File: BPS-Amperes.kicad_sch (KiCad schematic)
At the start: 35 parts, among them J1 Conn_02x10_Odd_Even, J2 ShuntConn, J3 PassthroughConn, J4 TestConn, J5 Conn_01x02, U1 INA186A3IDDFT, U2 OPA2196, U4 REF1930AIDDCT

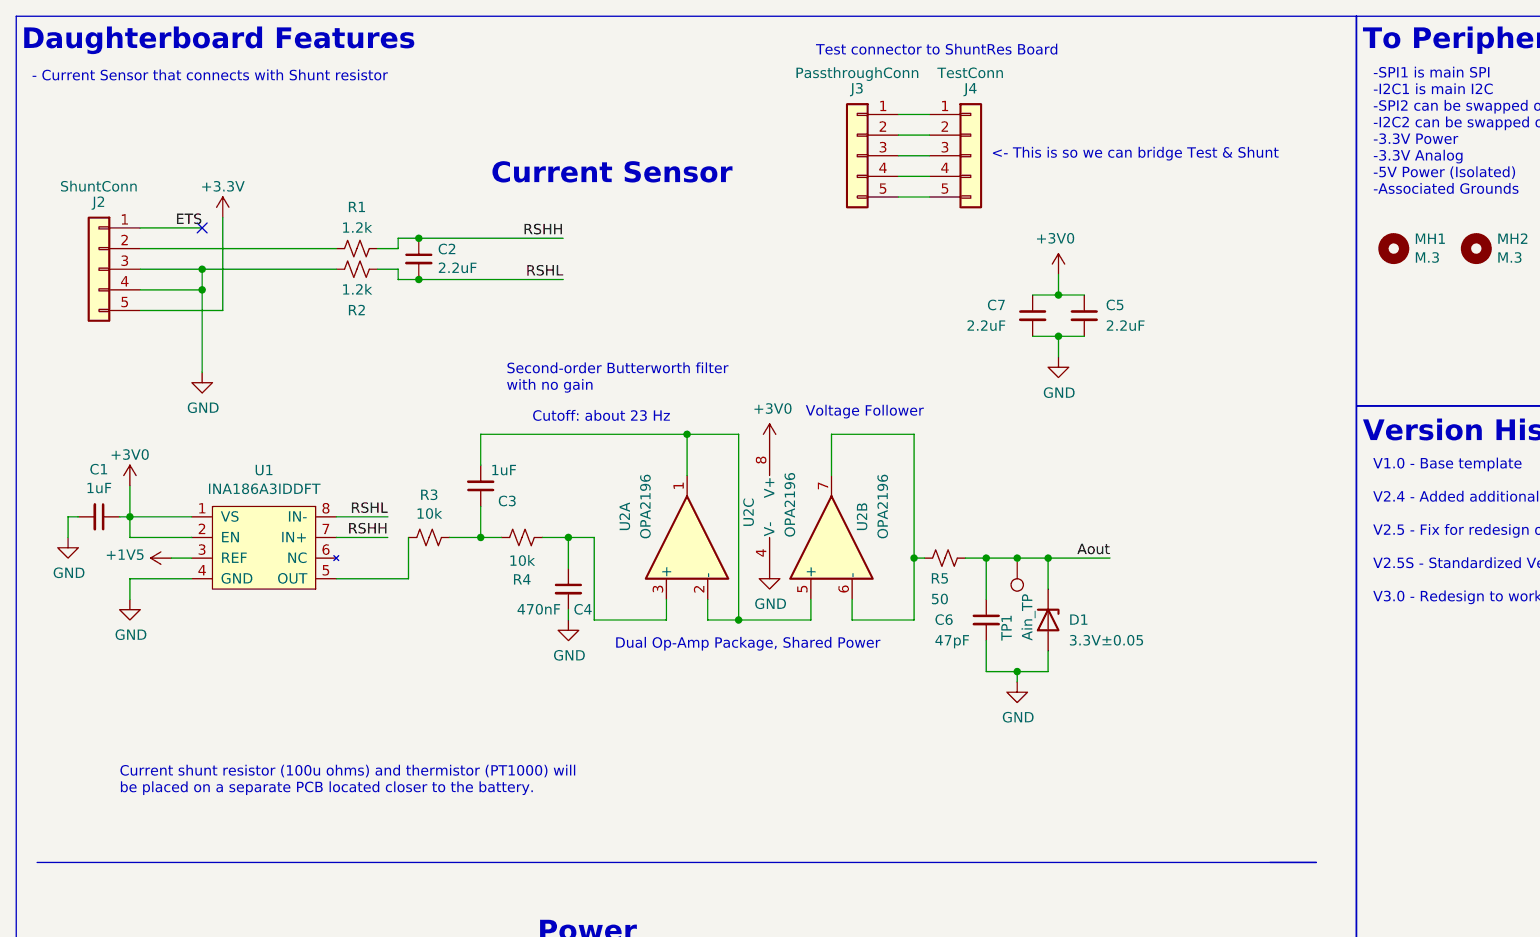
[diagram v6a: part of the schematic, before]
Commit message: Moved power components to the front and increased spacing between components
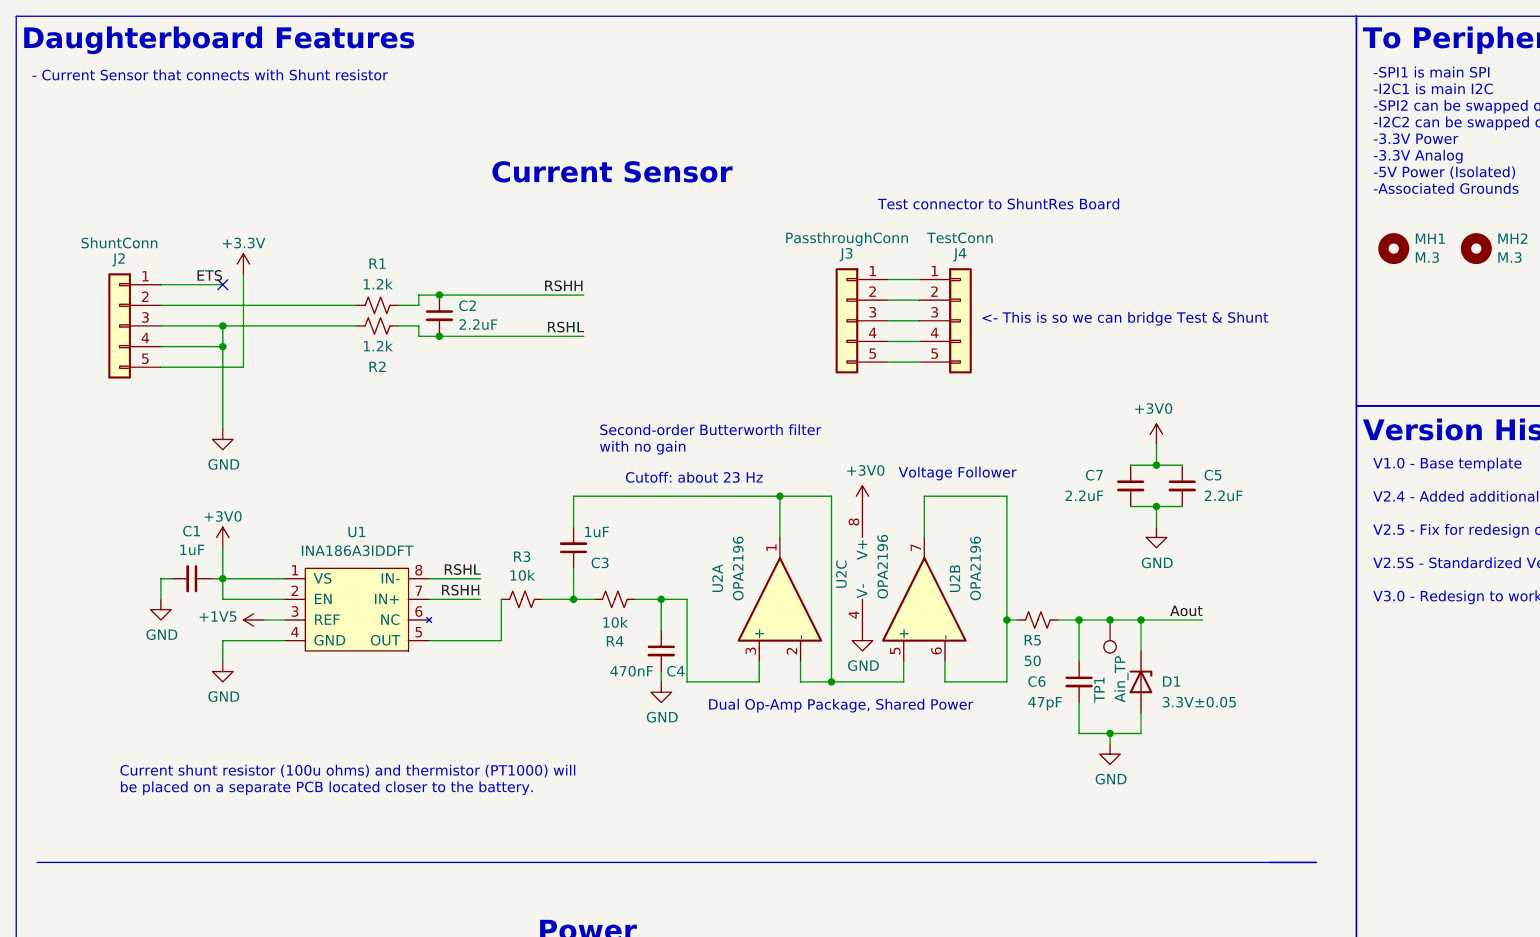
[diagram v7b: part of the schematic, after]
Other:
- moved on the sheet: C1, C2, C3, C4, C5, C6, C7, D1, J2, J3, J4, R1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

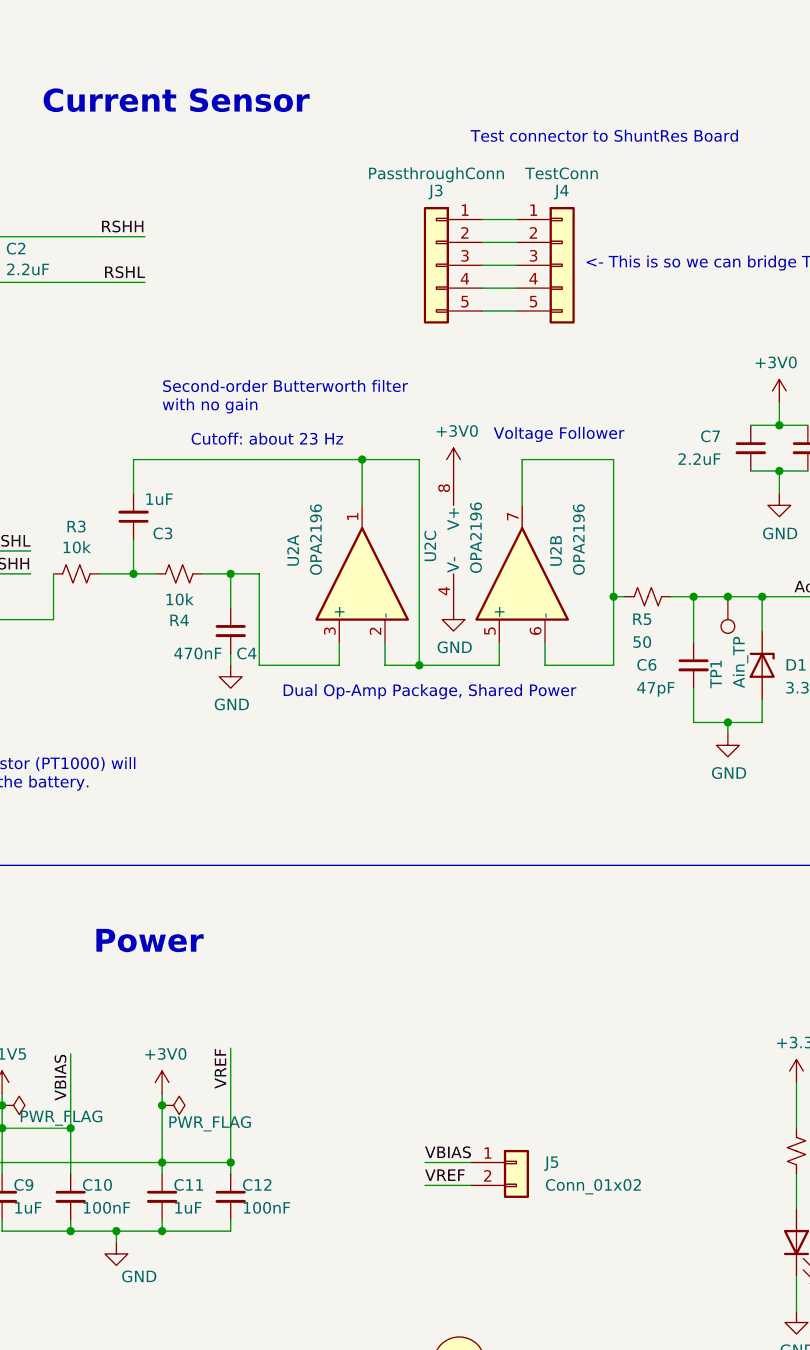
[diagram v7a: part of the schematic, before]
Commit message: Changed position of headers and labelled stuff
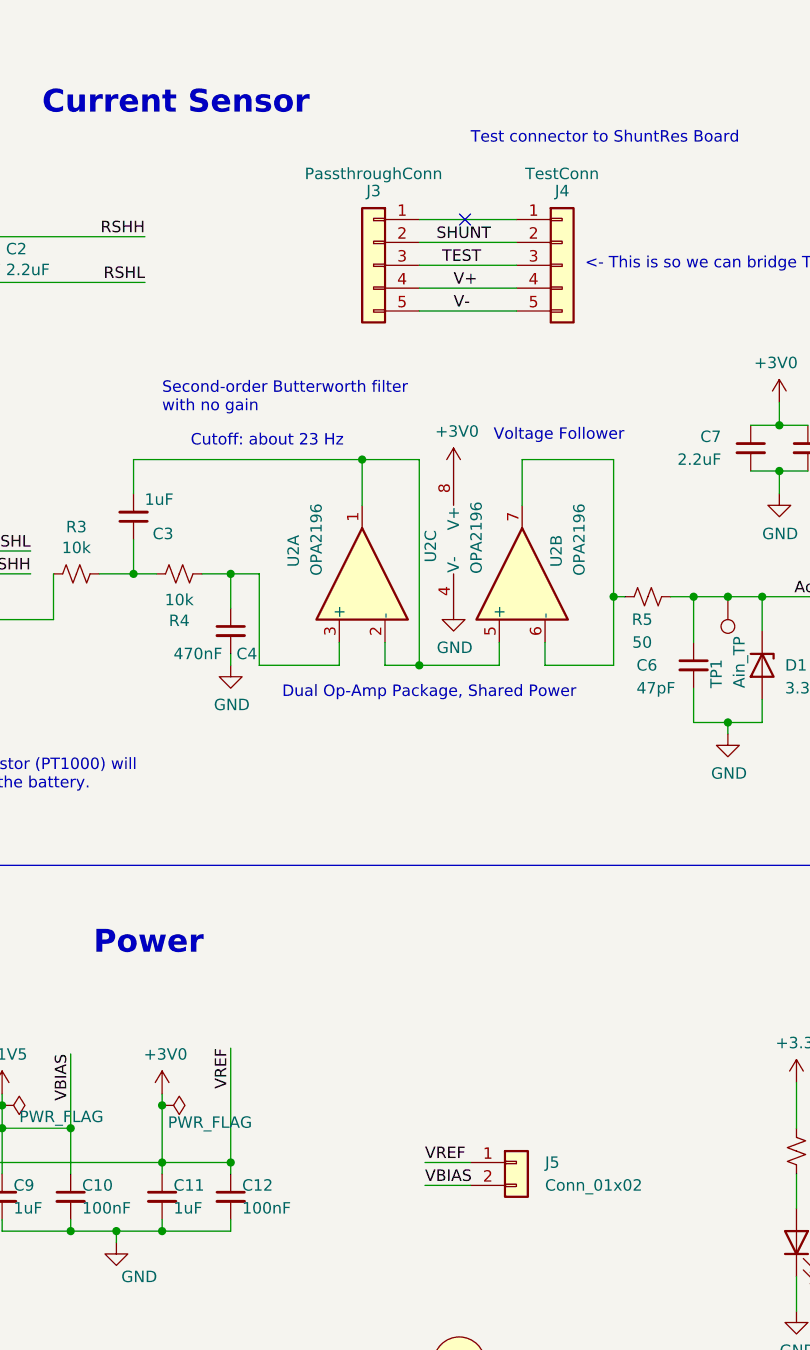
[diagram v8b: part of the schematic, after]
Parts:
- J4: footprint Connector_PinSocket_2.54mm:PinSocket_1x05_P2.54mm_Horizontal -> Connector_PinHeader_2.54mm:PinHeader_1x05_P2.54mm_Horizontal
- J5: footprint Connector_PinSocket_2.54mm:PinSocket_1x02_P2.54mm_Horizontal -> Connector_PinHeader_2.54mm:PinHeader_1x02_P2.54mm_Horizontal
- TP1: footprint Connector_PinSocket_2.54mm:PinSocket_1x01_P2.54mm_Horizontal -> Connector_PinHeader_2.54mm:PinHeader_1x01_P2.54mm_Horizontal
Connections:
- net +1V5: now also J5.2 (Pin_2); no longer J5.1 (Pin_1)
- net +3V0: now also J5.1 (Pin_1); no longer J5.2 (Pin_2)
- net SHUNT: now reaches J3.2 (Pin_2), J4.2 (Pin_2)
- net TEST: now reaches J3.3 (Pin_3), J4.3 (Pin_3)
- net V+: now reaches J3.4 (Pin_4), J4.4 (Pin_4)
- net V-: now reaches J3.5 (Pin_5), J4.5 (Pin_5)
- no-connect marks 14 -> 15
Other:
- moved on the sheet: J3
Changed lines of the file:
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@@
   (no_connect (at 239.395 43.18))
   (no_connect (at 257.81 43.18))
+  (no_connect (at 117.475 44.45))
   (no_connect (at 239.395 48.26))
   (no_connect (at 257.81 45.72))
@@
     (stroke (width 0) (type default))
   )
-  (wire (pts (xy 119.38 46.99) (xy 123.19 46.99))
+  (wire (pts (xy 112.395 46.99) (xy 123.19 46.99))
     (stroke (width 0) (type default))
   )
@@
     (stroke (width 0) (type default))
   )
-  (wire (pts (xy 119.38 52.07) (xy 123.19 52.07))
+  (wire (pts (xy 112.395 52.07) (xy 123.19 52.07))
     (stroke (width 0) (type default))
   )
@@
     (stroke (width 0) (type default))
   )
-  (wire (pts (xy 119.38 54.61) (xy 123.19 54.61))
+  (wire (pts (xy 112.395 54.61) (xy 123.19 54.61))
     (stroke (width 0) (type default))
   )
@@
     (stroke (width 0) (type default))
   )
-  (wire (pts (xy 119.38 44.45) (xy 123.19 44.45))
+  (wire (pts (xy 112.395 44.45) (xy 123.19 44.45))
     (stroke (width 0) (type default))
   )
@@
     (stroke (width 0) (type default))
   )
-  (wire (pts (xy 119.38 49.53) (xy 123.19 49.53))
+  (wire (pts (xy 112.395 49.53) (xy 123.19 49.53))
     (stroke (width 0) (type default))
   )
@@
     (effects (font (size 1.27 1.27)) (justify right bottom))
   )
-  (label "VBIAS" (at 113.03 149.225 0) (fields_autoplaced)
+  (label "VBIAS" (at 113.03 151.765 0) (fields_autoplaced)
     (effects (font (size 1.27 1.27)) (justify left bottom))
   )
@@
     (effects (font (size 1.27 1.27)) (justify left bottom))
   )
+  (label "V+" (at 116.205 52.07 0) (fields_autoplaced)
+    (effects (font (size 1.27 1.27)) (justify left bottom))
+  )
   (label "RSHL" (at 81.915 51.435 180) (fields_autoplaced)
     (effects (font (size 1.27 1.27)) (justify right bottom))
@@
     (effects (font (size 1.27 1.27)) (justify right bottom))
   )
+  (label "V-" (at 116.205 54.61 0) (fields_autoplaced)
+    (effects (font (size 1.27 1.27)) (justify left bottom))
+  )
   (label "SPI1_MISO" (at 239.395 43.18 180) (fields_autoplaced)
     (effects (font (size 1.27 1.27)) (justify right bottom))
@@
     (effects (font (size 1.27 1.27)) (justify left bottom))
   )
-  (label "VREF" (at 113.03 151.765 0) (fields_autoplaced)
+  (label "VREF" (at 113.03 149.225 0) (fields_autoplaced)
     (effects (font (size 1.27 1.27)) (justify left bottom))
   )
@@
   (label "SPI1_SCK" (at 238.76 40.64 180) (fields_autoplaced)
     (effects (font (size 1.27 1.27)) (justify right bottom))
+  )
+  (label "SHUNT" (at 114.3 46.99 0) (fields_autoplaced)
+    (effects (font (size 1.27 1.27)) (justify left bottom))
+  )
+  (label "TEST" (at 114.935 49.53 0) (fields_autoplaced)
+    (effects (font (size 1.27 1.27)) (justify left bottom))
   )
   (label "I2C1_SCL" (at 257.81 40.64 0) (fields_autoplaced)
@@
       (effects (font (size 1.27 1.27)))
     )
-    (property "Footprint" "Connector_PinSocket_2.54mm:PinSocket_1x05_P2.54mm_Horizontal" (at 128.27 49.53 0)
+    (property "Footprint" "Connector_PinHeader_2.54mm:PinHeader_1x05_P2.54mm_Horizontal" (at 128.27 49.53 0)
       (effects (font (size 1.27 1.27)) hide)
     )
@@
       (effects (font (size 1.27 1.27)) (justify right))
     )
-    (property "Footprint" "Connector_PinSocket_2.54mm:PinSocket_1x01_P2.54mm_Horizontal" (at 141.605 86.36 0)
+    (property "Footprint" "Connector_PinHeader_2.54mm:PinHeader_1x01_P2.54mm_Horizontal" (at 141.605 86.36 0)
       (effects (font (size 1.27 1.27)) hide)
     )
@@
       (effects (font (size 1.27 1.27)) (justify left))
     )
-    (property "Footprint" "Connector_PinSocket_2.54mm:PinSocket_1x02_P2.54mm_Horizontal" (at 123.19 149.225 0)
+    (property "Footprint" "Connector_PinHeader_2.54mm:PinHeader_1x02_P2.54mm_Horizontal" (at 123.19 149.225 0)
       (effects (font (size 1.27 1.27)) hide)
     )
@@
     )
   )
-  (symbol (lib_id "Connector_Generic:Conn_01x05") (at 114.3 49.53 0) (mirror y) (unit 1)
-    (in_bom yes) (on_board yes) (dnp no)
-    (property "Reference" "J3" (at 114.3 41.275 0)
-      (effects (font (size 1.27 1.27)))
-    )
-    (property "Value" "PassthroughConn" (at 114.3 39.37 0)
-      (effects (font (size 1.27 1.27)))
-    )
-    (property "Footprint" "Connector_PinSocket_2.54mm:PinSocket_1x05_P2.54mm_Vertical" (at 114.3 49.53 0)
-      (effects (font (size 1.27 1.27)) hide)
-    )
-    (property "Datasheet" "~" (at 114.3 49.53 0)
-      (effects (font (size 1.27 1.27)) hide)
-    )
+  (symbol (lib_id "Connector_Generic:Conn_01x05") (at 107.315 49.53 0) (mirror y) (unit 1)
+    (in_bom yes) (on_board yes) (dnp no)
+    (property "Reference" "J3" (at 107.315 41.275 0)
+      (effects (font (size 1.27 1.27)))
+    )
+    (property "Value" "PassthroughConn" (at 107.315 39.37 0)
+      (effects (font (size 1.27 1.27)))
+    )
+    (property "Footprint" "Connector_PinSocket_2.54mm:PinSocket_1x05_P2.54mm_Vertical" (at 107.315 49.53 0)
+      (effects (font (size 1.27 1.27)) hide)
+    )
+    (property "Datasheet" "~" (at 107.315 49.53 0)
+      (effects (font (size 1.27 1.27)) hide)
+    )
